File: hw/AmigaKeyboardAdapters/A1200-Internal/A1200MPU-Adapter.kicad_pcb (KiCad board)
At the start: 2 copper layers, 30.5 x 31.1 mm, 8 parts, among them P1 CONN_02X03, U1 A1200U13_REV_PLCC44

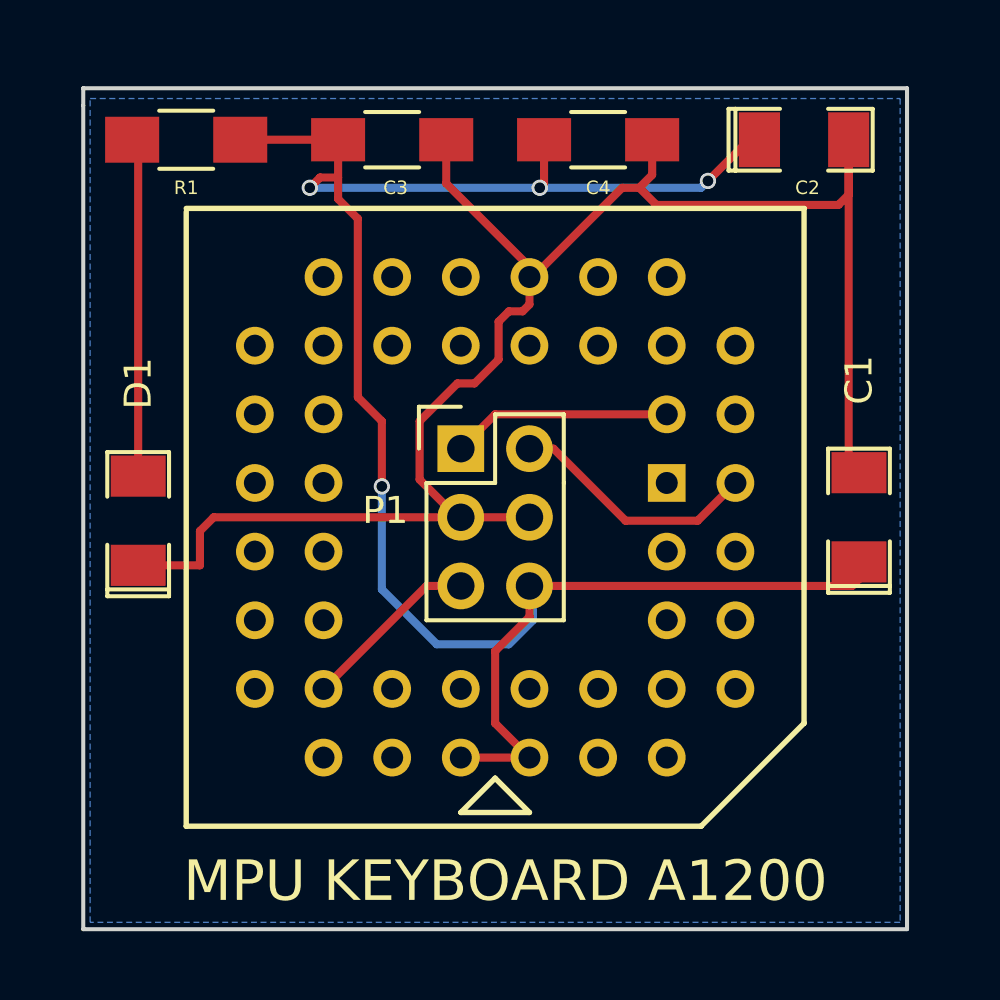
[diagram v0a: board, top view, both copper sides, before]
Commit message: Added the idc 2x3 box
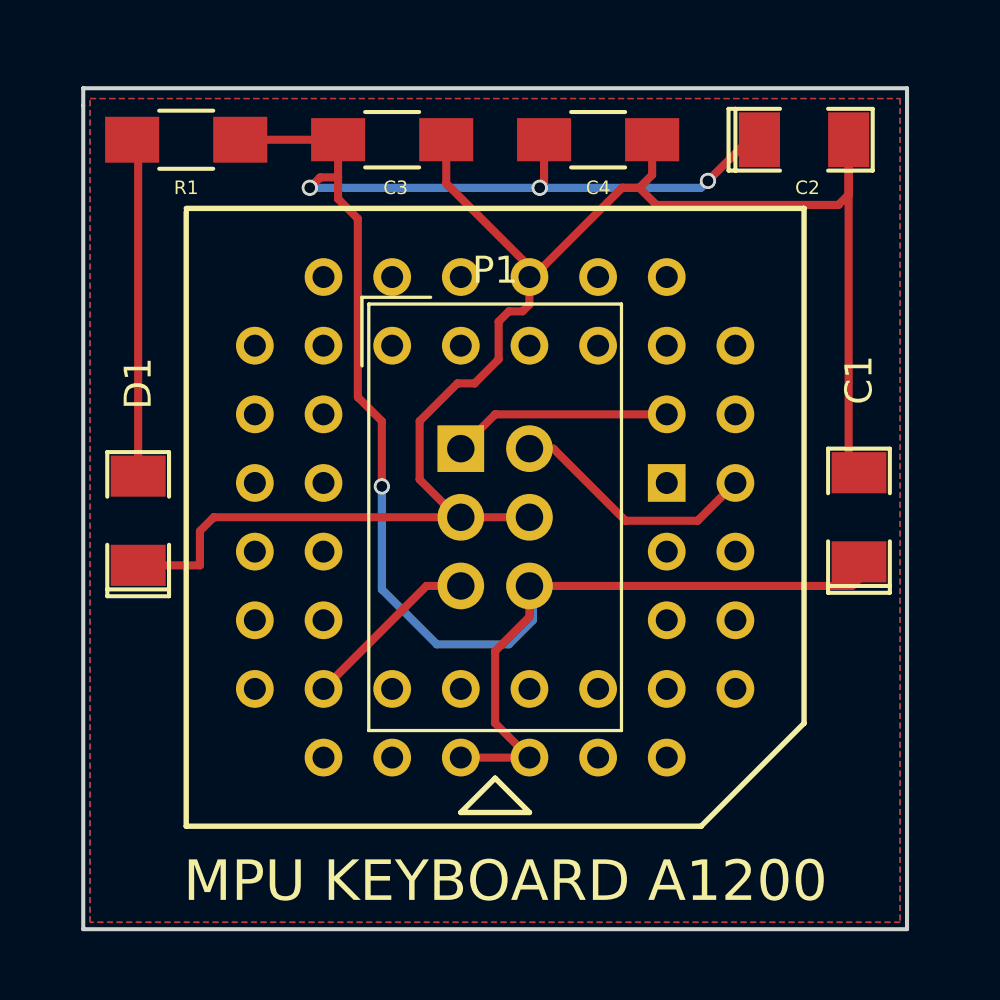
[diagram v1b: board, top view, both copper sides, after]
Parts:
- P1: footprint Pin_Headers:Pin_Header_Straight_2x03 -> RetroBitLab:IDC-Header_2x03_P2.54mm_Vertical
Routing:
- added copper zone on F.Cu, net GND
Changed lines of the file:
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@@
-    )
-  )
-  (module Pin_Headers:Pin_Header_Straight_2x03 (layer F.Cu)
-    (at 146.05 101.6)
-    (descr "Through hole pin header")
-    (tags "pin header")
-    (fp_text reference P1 (at -2.794 2.286) (layer F.SilkS)
-      (effects (font (size 1 1) (thickness 0.15)))
-    )
-    (fp_text value CONN_02X03 (at 0 -3.1) (layer F.Fab)
-      (effects (font (size 1 1) (thickness 0.15)))
-    )
-    (fp_line (start -1.27 1.27) (end -1.27 6.35) (layer F.SilkS) (width 0.15))
-    (fp_line (start -1.55 -1.55) (end 0 -1.55) (layer F.SilkS) (width 0.15))
-    (fp_line (start -1.75 -1.75) (end -1.75 6.85) (layer F.CrtYd) (width 0.05))
-    (fp_line (start 4.3 -1.75) (end 4.3 6.85) (layer F.CrtYd) (width 0.05))
-    (fp_line (start -1.75 -1.75) (end 4.3 -1.75) (layer F.CrtYd) (width 0.05))
-    (fp_line (start -1.75 6.85) (end 4.3 6.85) (layer F.CrtYd) (width 0.05))
-    (fp_line (start 1.27 -1.27) (end 1.27 1.27) (layer F.SilkS) (width 0.15))
-    (fp_line (start 1.27 1.27) (end -1.27 1.27) (layer F.SilkS) (width 0.15))
-    (fp_line (start -1.27 6.35) (end 3.81 6.35) (layer F.SilkS) (width 0.15))
-    (fp_line (start 3.81 6.35) (end 3.81 1.27) (layer F.SilkS) (width 0.15))
-    (fp_line (start -1.55 -1.55) (end -1.55 0) (layer F.SilkS) (width 0.15))
-    (fp_line (start 3.81 -1.27) (end 1.27 -1.27) (layer F.SilkS) (width 0.15))
-    (fp_line (start 3.81 1.27) (end 3.81 -1.27) (layer F.SilkS) (width 0.15))
-    (pad 1 thru_hole rect (at 0 0) (size 1.7272 1.7272) (drill 1.016) (layers *.Cu *.Mask F.SilkS)
-      (net 4 mKBD_CLOCK))
-    (pad 2 thru_hole oval (at 2.54 0) (size 1.7272 1.7272) (drill 1.016) (layers *.Cu *.Mask F.SilkS)
-      (net 5 mKBD_DATA))
-    (pad 3 thru_hole oval (at 0 2.54) (size 1.7272 1.7272) (drill 1.016) (layers *.Cu *.Mask F.SilkS)
-      (net 2 GND))
-    (pad 4 thru_hole oval (at 2.54 2.54) (size 1.7272 1.7272) (drill 1.016) (layers *.Cu *.Mask F.SilkS)
-      (net 2 GND))
-    (pad 5 thru_hole oval (at 0 5.08) (size 1.7272 1.7272) (drill 1.016) (layers *.Cu *.Mask F.SilkS)
-      (net 6 mKBD_RESET))
-    (pad 6 thru_hole oval (at 2.54 5.08) (size 1.7272 1.7272) (drill 1.016) (layers *.Cu *.Mask F.SilkS)
-      (net 1 VCC5V))
-    (model Pin_Headers.3dshapes/Pin_Header_Straight_2x03.wrl
-      (at (xyz 0.05 -0.1 0))
-      (scale (xyz 1 1 1))
-      (rotate (xyz 0 0 90))
     )
   )
@@
       (at (xyz 0 0 0))
       (scale (xyz 0.17 0.16 0.16))
+      (rotate (xyz 0 0 0))
+    )
+  )
+  (module RetroBitLab:IDC-Header_2x03_P2.54mm_Vertical (layer F.Cu)
+    (at 146.05 101.6)
+    (descr "Through hole straight IDC box header, 2x03, 2.54mm pitch, double rows")
+    (tags "Through hole IDC box header THT 2x03 2.54mm double row")
+    (fp_text reference P1 (at 1.27 -6.604) (layer F.SilkS)
+      (effects (font (size 1 1) (thickness 0.15)))
+    )
+    (fp_text value CONN_02X03 (at 1.27 11.684) (layer F.Fab)
+      (effects (font (size 1 1) (thickness 0.15)))
+    )
+    (fp_text user %R (at 1.27 2.54) (layer F.Fab)
+      (effects (font (size 1 1) (thickness 0.15)))
+    )
+    (fp_line (start 5.695 -5.1) (end 5.695 10.18) (layer F.Fab) (width 0.1))
+    (fp_line (start 5.145 -4.56) (end 5.145 9.62) (layer F.Fab) (width 0.1))
+    (fp_line (start -3.155 -5.1) (end -3.155 10.18) (layer F.Fab) (width 0.1))
+    (fp_line (start -2.605 -4.56) (end -2.605 0.29) (layer F.Fab) (width 0.1))
+    (fp_line (start -2.605 4.79) (end -2.605 9.62) (layer F.Fab) (width 0.1))
+    (fp_line (start -2.605 0.29) (end -3.155 0.29) (layer F.Fab) (width 0.1))
+    (fp_line (start -2.605 4.79) (end -3.155 4.79) (layer F.Fab) (width 0.1))
+    (fp_line (start 5.695 -5.1) (end -3.155 -5.1) (layer F.Fab) (width 0.1))
+    (fp_line (start 5.145 -4.56) (end -2.605 -4.56) (layer F.Fab) (width 0.1))
+    (fp_line (start 5.695 10.18) (end -3.155 10.18) (layer F.Fab) (width 0.1))
+    (fp_line (start 5.145 9.62) (end -2.605 9.62) (layer F.Fab) (width 0.1))
+    (fp_line (start 5.695 -5.1) (end 5.145 -4.56) (layer F.Fab) (width 0.1))
+    (fp_line (start 5.695 10.18) (end 5.145 9.62) (layer F.Fab) (width 0.1))
+    (fp_line (start -3.155 -5.1) (end -2.605 -4.56) (layer F.Fab) (width 0.1))
+    (fp_line (start -3.155 10.18) (end -2.605 9.62) (layer F.Fab) (width 0.1))
+    (fp_line (start 5.95 -5.35) (end 5.95 10.43) (layer F.CrtYd) (width 0.05))
+    (fp_line (start 5.95 10.43) (end -3.41 10.43) (layer F.CrtYd) (width 0.05))
+    (fp_line (start -3.41 10.43) (end -3.41 -5.35) (layer F.CrtYd) (width 0.05))
+    (fp_line (start -3.41 -5.35) (end 5.95 -5.35) (layer F.CrtYd) (width 0.05))
+    (fp_line (start 5.945 -5.35) (end 5.945 10.43) (layer F.SilkS) (width 0.12))
+    (fp_line (start 5.945 10.43) (end -3.405 10.43) (layer F.SilkS) (width 0.12))
+    (fp_line (start -3.405 10.43) (end -3.405 -5.35) (layer F.SilkS) (width 0.12))
+    (fp_line (start -3.405 -5.35) (end 5.945 -5.35) (layer F.SilkS) (width 0.12))
+    (fp_line (start -3.655 -5.6) (end -3.655 -3.06) (layer F.SilkS) (width 0.12))
+    (fp_line (start -3.655 -5.6) (end -1.115 -5.6) (layer F.SilkS) (width 0.12))
+    (pad 1 thru_hole rect (at 0 0) (size 1.7272 1.7272) (drill 1.016) (layers *.Cu *.Mask)
+      (net 4 mKBD_CLOCK))
+    (pad 2 thru_hole oval (at 2.54 0) (size 1.7272 1.7272) (drill 1.016) (layers *.Cu *.Mask)
+      (net 5 mKBD_DATA))
+    (pad 3 thru_hole oval (at 0 2.54) (size 1.7272 1.7272) (drill 1.016) (layers *.Cu *.Mask)
+      (net 2 GND))
+    (pad 4 thru_hole oval (at 2.54 2.54) (size 1.7272 1.7272) (drill 1.016) (layers *.Cu *.Mask)
+      (net 2 GND))
+    (pad 5 thru_hole oval (at 0 5.08) (size 1.7272 1.7272) (drill 1.016) (layers *.Cu *.Mask)
+      (net 6 mKBD_RESET))
+    (pad 6 thru_hole oval (at 2.54 5.08) (size 1.7272 1.7272) (drill 1.016) (layers *.Cu *.Mask)
+      (net 1 VCC5V))
+    (model /home/debian/packages/kicad/kicad-packages3D/Connector_IDC.3dshapes/IDC-Header_2x03_P2.54mm_Vertical.wrl
+      (at (xyz 0 0 0))
+      (scale (xyz 1 1 1))
       (rotate (xyz 0 0 0))
     )
@@
     (connect_pads (clearance 0.508))
     (min_thickness 0.254)
+    (fill yes (arc_segments 16) (thermal_gap 0.508) (thermal_bridge_width 0.508))
+    (polygon
+      (pts
+        (xy 162.306 119.126) (xy 132.334 119.126) (xy 132.334 88.646) (xy 162.306 88.646) (xy 162.306 119.126)
+      )
+    )
+  )
+  (zone (net 2) (net_name GND) (layer F.Cu) (hatch edge 0.508)
+    (connect_pads (clearance 0.508))
+    (min_thickness 0.254)

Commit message: Removed
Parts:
- C1, C2: footprint SMD_Packages:SMD-1206_Pol -> Capacitor_Tantalum_SMD:CP_EIA-3216-12_Kemet-S_Pad1.58x1.35mm_HandSolder
- C3, C4: footprint Capacitors_SMD:C_1206_HandSoldering -> Capacitor_SMD:C_1206_3216Metric_Pad1.33x1.80mm_HandSolder
- D1: value Led_Small -> RED; footprint SMD_Packages:SMD-1206_Pol -> LED_SMD:LED_1206_3216Metric_Pad1.42x1.75mm_HandSolder
- P1: value CONN_02X03 -> Conn_02x03_Odd_Even; footprint RetroBitLab:IDC-Header_2x03_P2.54mm_Vertical -> Connector_IDC:IDC-Header_2x03_P2.54mm_Vertical
- R1: value 330 -> 330R; footprint Resistors_SMD:R_1206_HandSoldering -> Resistor_SMD:R_1206_3216Metric_Pad1.30x1.75mm_HandSolder
- U1: footprint Sockets:PLCC44 -> RetroBitLab:PLCC-44_THT-Socket_3D
- moved U1 6.43 mm to (153.7, 103.1), turned to 90 degrees
- moved D1 0.40 mm to (133.7, 104.1)
- moved P1 0.25 mm to (146.1, 101.9)
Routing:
- net VCC5V: track 72.3 -> 66.2 mm, vias 4 -> 0
- net GND: track 64.3 -> 61.1 mm
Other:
- rule pad_to_mask_clearance: 0.2 -> 0
- board text added: "designed by R.G.2018/2022"
- board text removed: "designed by R.G.2018"
